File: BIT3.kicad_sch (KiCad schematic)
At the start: 39 parts, among them J1 Conn_02x04_Odd_Even, J2 Conn_01x02_Pin, Q1 2SC1815, SW1 SW_SPDT, SW2 SW_Push, SW3 SW_Push, U2 SG-107F, U3 SG-107F, U4 SG-107F, U5 SG-107F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

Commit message: Update PCB Design
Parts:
- added R17, R18, R19, R20, R21: R, Resistor_THT:R_Axial_DIN0204_L3.6mm_D1.6mm_P7.62mm_Horizontal, symbol Device:R
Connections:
- net +BATT: now also R17.1; no longer U7.8 (CH7)
- net GND: now also R21.2
- new net: R17.2, R18.1
- new net: R20.2, R21.1, U7.8 (CH7)
- new net: R18.2, R19.1
- new net: R19.2, R20.1
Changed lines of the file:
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@@
   (junction (at 163.83 127) (diameter 0) (color 0 0 0 0)
+  )
+  (junction (at 16.51 152.4) (diameter 0) (color 0 0 0 0)
   )
   (junction (at 97.79 143.51) (diameter 0) (color 0 0 0 0)
@@
     (stroke (width 0) (type default))
   )
+  (wire (pts (xy 16.51 152.4) (xy 36.83 152.4))
+    (stroke (width 0) (type default))
+  )
   (wire (pts (xy 88.9 76.2) (xy 91.44 76.2))
     (stroke (width 0) (type default))
@@
     (effects (font (size 1.27 1.27)) (justify right bottom))
   )
+  (label "V_Battery" (at 16.51 121.92 0) (fields_autoplaced)
+    (effects (font (size 1.27 1.27)) (justify left bottom))
+  )
   (label "DRV8835_AIN2" (at 147.32 101.6 180) (fields_autoplaced)
     (effects (font (size 1.27 1.27)) (justify right bottom))
@@
     (effects (font (size 1.27 1.27)) (justify left bottom))
   )
-  (label "V_Battery" (at 36.83 152.4 180) (fields_autoplaced)
-    (effects (font (size 1.27 1.27)) (justify right bottom))
-  )
   (label "LED_CL" (at 203.2 76.2 0) (fields_autoplaced)
     (effects (font (size 1.27 1.27)) (justify left bottom))
@@
     (pin "1")
     (pin "2")
+    (pin "3")
     (pin "4")
-    (pin "3")
     (instances
       (project "BIT3"
@@
         (path "/e911d5a5-765c-4e39-aa6a-9a13739432fd"
           (reference "R5") (unit 1)
+        )
+      )
+    )
+  )
+  (symbol (lib_id "power:GND") (at 16.51 160.02 0) (unit 1)
+    (in_bom yes) (on_board yes) (dnp no) (fields_autoplaced)
+    (property "Reference" "#PWR024" (at 16.51 166.37 0)
+      (effects (font (size 1.27 1.27)) hide)
+    )
+    (property "Value" "GND" (at 16.51 165.1 0)
+      (effects (font (size 1.27 1.27)))
+    )
+    (property "Footprint" "" (at 16.51 160.02 0)
+      (effects (font (size 1.27 1.27)) hide)
+    )
+    (property "Datasheet" "" (at 16.51 160.02 0)
+      (effects (font (size 1.27 1.27)) hide)
+    )
+    (pin "1")
+    (instances
+      (project "BIT3"
+        (path "/e911d5a5-765c-4e39-aa6a-9a13739432fd"
+          (reference "#PWR024") (unit 1)
+        )
+      )
+    )
+  )
+  (symbol (lib_id "Device:R") (at 16.51 125.73 0) (unit 1)
+    (in_bom yes) (on_board yes) (dnp no) (fields_autoplaced)
+    (property "Reference" "R17" (at 19.05 125.095 0)
+      (effects (font (size 1.27 1.27)) (justify left))
+    )
+    (property "Value" "R" (at 19.05 127.635 0)
+      (effects (font (size 1.27 1.27)) (justify left))
+    )
+    (property "Footprint" "Resistor_THT:R_Axial_DIN0204_L3.6mm_D1.6mm_P7.62mm_Horizontal" (at 14.732 125.73 90)
+      (effects (font (size 1.27 1.27)) hide)
+    )
+    (property "Datasheet" "~" (at 16.51 125.73 0)
+      (effects (font (size 1.27 1.27)) hide)
+    )
+    (pin "1")
+    (pin "2")
+    (instances
+      (project "BIT3"
+        (path "/e911d5a5-765c-4e39-aa6a-9a13739432fd"
+          (reference "R17") (unit 1)
         )
       )
@@
     )
   )
+  (symbol (lib_id "Device:R") (at 16.51 156.21 0) (unit 1)
+    (in_bom yes) (on_board yes) (dnp no) (fields_autoplaced)
+    (property "Reference" "R21" (at 19.05 155.575 0)
+      (effects (font (size 1.27 1.27)) (justify left))
+    )
+    (property "Value" "R" (at 19.05 158.115 0)
+      (effects (font (size 1.27 1.27)) (justify left))
+    )
+    (property "Footprint" "Resistor_THT:R_Axial_DIN0204_L3.6mm_D1.6mm_P7.62mm_Horizontal" (at 14.732 156.21 90)
+      (effects (font (size 1.27 1.27)) hide)
+    )
+    (property "Datasheet" "~" (at 16.51 156.21 0)
+      (effects (font (size 1.27 1.27)) hide)
+    )
+    (pin "1")
+    (pin "2")
+    (instances
+      (project "BIT3"
+        (path "/e911d5a5-765c-4e39-aa6a-9a13739432fd"
+          (reference "R21") (unit 1)
+        )
+      )
+    )
+  )
   (symbol (lib_id "Device:C") (at 233.68 128.27 0) (unit 1)
     (in_bom yes) (on_board yes) (dnp no) (fields_autoplaced)
@@
         (path "/e911d5a5-765c-4e39-aa6a-9a13739432fd"
           (reference "U4") (unit 1)
+        )
+      )
+    )
+  )
+  (symbol (lib_id "Device:R") (at 16.51 133.35 0) (unit 1)
+    (in_bom yes) (on_board yes) (dnp no) (fields_autoplaced)
+    (property "Reference" "R18" (at 19.05 132.715 0)
+      (effects (font (size 1.27 1.27)) (justify left))
+    )
+    (property "Value" "R" (at 19.05 135.255 0)
+      (effects (font (size 1.27 1.27)) (justify left))
+    )
+    (property "Footprint" "Resistor_THT:R_Axial_DIN0204_L3.6mm_D1.6mm_P7.62mm_Horizontal" (at 14.732 133.35 90)
+      (effects (font (size 1.27 1.27)) hide)
+    )
+    (property "Datasheet" "~" (at 16.51 133.35 0)
+      (effects (font (size 1.27 1.27)) hide)
+    )
+    (pin "1")
+    (pin "2")
+    (instances
+      (project "BIT3"
+        (path "/e911d5a5-765c-4e39-aa6a-9a13739432fd"
+          (reference "R18") (unit 1)
         )
       )
@@
     )
   )
+  (symbol (lib_id "Device:R") (at 16.51 148.59 0) (unit 1)
+    (in_bom yes) (on_board yes) (dnp no) (fields_autoplaced)
+    (property "Reference" "R20" (at 19.05 147.955 0)
+      (effects (font (size 1.27 1.27)) (justify left))
+    )
+    (property "Value" "R" (at 19.05 150.495 0)
+      (effects (font (size 1.27 1.27)) (justify left))
+    )
+    (property "Footprint" "Resistor_THT:R_Axial_DIN0204_L3.6mm_D1.6mm_P7.62mm_Horizontal" (at 14.732 148.59 90)
+      (effects (font (size 1.27 1.27)) hide)
+    )
+    (property "Datasheet" "~" (at 16.51 148.59 0)
+      (effects (font (size 1.27 1.27)) hide)
+    )
+    (pin "1")
+    (pin "2")
+    (instances
+      (project "BIT3"
+        (path "/e911d5a5-765c-4e39-aa6a-9a13739432fd"
+          (reference "R20") (unit 1)
+        )
+      )
+    )
+  )
   (symbol (lib_id "Device:R") (at 226.06 80.01 0) (unit 1)
     (in_bom yes) (on_board yes) (dnp no) (fields_autoplaced)
@@
         )
       )
+    )
+  )
+  (symbol (lib_id "Device:R") (at 16.51 140.97 0) (unit 1)
+    (in_bom yes) (on_board yes) (dnp no) (fields_autoplaced)
+    (property "Reference" "R19" (at 19.05 140.335 0)
+      (effects (font (size 1.27 1.27)) (justify left))
+    )
+    (property "Value" "R" (at 19.05 142.875 0)
+      (effects (font (size 1.27 1.27)) (justify left))
+    )
+    (property "Footprint" "Resistor_THT:R_Axial_DIN0204_L3.6mm_D1.6mm_P7.62mm_Horizontal" (at 14.732 140.97 90)
+      (effects (font (size 1.27 1.27)) hide)
+    )
+    (property "Datasheet" "~" (at 16.51 140.97 0)
+      (effects (font (size 1.27 1.27)) hide)
+    )
+    (pin "1")
+    (pin "2")
+    (instances
+      (project "BIT3"
+        (path "/e911d5a5-765c-4e39-aa6a-9a13739432fd"
+          (reference "R19") (unit 1)
+        )
+      )

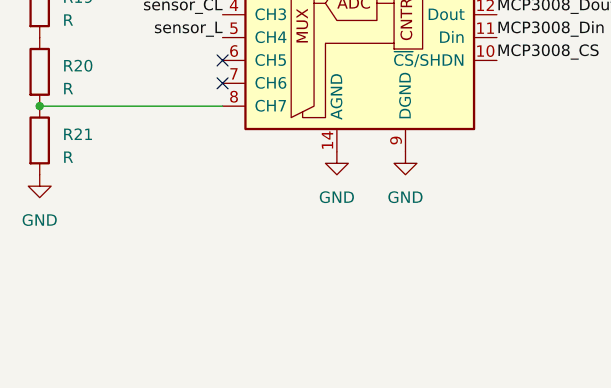
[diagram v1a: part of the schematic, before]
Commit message: 基板更新
MCP3008 にパスコンを追加
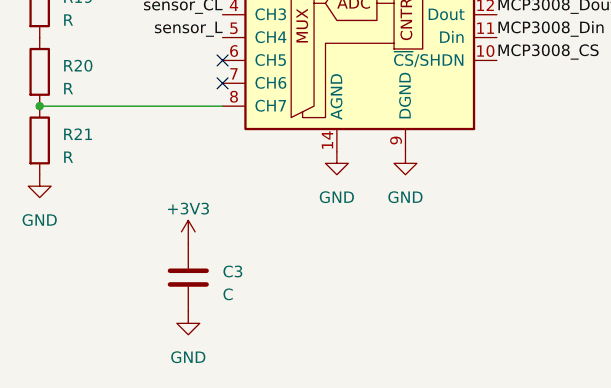
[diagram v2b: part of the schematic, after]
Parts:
- added C3: C, Capacitor_THT:C_Disc_D4.7mm_W2.5mm_P5.00mm, symbol Device:C
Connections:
- net +3V3: now also C3.1
- net GND: now also C3.2
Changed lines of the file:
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@@
+    )
+  )
+  (symbol (lib_id "power:+3V3") (at 33.02 167.64 0) (unit 1)
+    (in_bom yes) (on_board yes) (dnp no) (fields_autoplaced)
+    (property "Reference" "#PWR027" (at 33.02 171.45 0)
+      (effects (font (size 1.27 1.27)) hide)
+    )
+    (property "Value" "+3V3" (at 33.02 163.83 0)
+      (effects (font (size 1.27 1.27)))
+    )
+    (property "Footprint" "" (at 33.02 167.64 0)
+      (effects (font (size 1.27 1.27)) hide)
+    )
+    (property "Datasheet" "" (at 33.02 167.64 0)
+      (effects (font (size 1.27 1.27)) hide)
+    )
+    (pin "1")
+    (instances
+      (project "RP2040-BasicDesign"
+        (path "/14b941fc-8df0-4613-ad34-21e1e03e5f30"
+          (reference "#PWR027") (unit 1)
+        )
+      )
+      (project "BIT3"
+        (path "/e911d5a5-765c-4e39-aa6a-9a13739432fd"
+          (reference "#PWR025") (unit 1)
+        )
+      )
     )
   )
@@
         (path "/e911d5a5-765c-4e39-aa6a-9a13739432fd"
           (reference "#PWR08") (unit 1)
+        )
+      )
+    )
+  )
+  (symbol (lib_id "Device:C") (at 33.02 171.45 0) (unit 1)
+    (in_bom yes) (on_board yes) (dnp no) (fields_autoplaced)
+    (property "Reference" "C3" (at 36.83 170.815 0)
+      (effects (font (size 1.27 1.27)) (justify left))
+    )
+    (property "Value" "C" (at 36.83 173.355 0)
+      (effects (font (size 1.27 1.27)) (justify left))
+    )
+    (property "Footprint" "Capacitor_THT:C_Disc_D4.7mm_W2.5mm_P5.00mm" (at 33.9852 175.26 0)
+      (effects (font (size 1.27 1.27)) hide)
+    )
+    (property "Datasheet" "~" (at 33.02 171.45 0)
+      (effects (font (size 1.27 1.27)) hide)
+    )
+    (pin "1")
+    (pin "2")
+    (instances
+      (project "BIT3"
+        (path "/e911d5a5-765c-4e39-aa6a-9a13739432fd"
+          (reference "C3") (unit 1)
         )
       )
@@
         )
       )
+    )
+  )
+  (symbol (lib_id "power:GND") (at 33.02 175.26 0) (unit 1)
+    (in_bom yes) (on_board yes) (dnp no) (fields_autoplaced)
+    (property "Reference" "#PWR026" (at 33.02 181.61 0)
+      (effects (font (size 1.27 1.27)) hide)
+    )
+    (property "Value" "GND" (at 33.02 180.34 0)
+      (effects (font (size 1.27 1.27)))
+    )
+    (property "Footprint" "" (at 33.02 175.26 0)
+      (effects (font (size 1.27 1.27)) hide)
+    )
+    (property "Datasheet" "" (at 33.02 175.26 0)
+      (effects (font (size 1.27 1.27)) hide)
+    )
+    (pin "1")
+    (instances
+      (project "BIT3"
+        (path "/e911d5a5-765c-4e39-aa6a-9a13739432fd"
+          (reference "#PWR026") (unit 1)
+        )
+      )

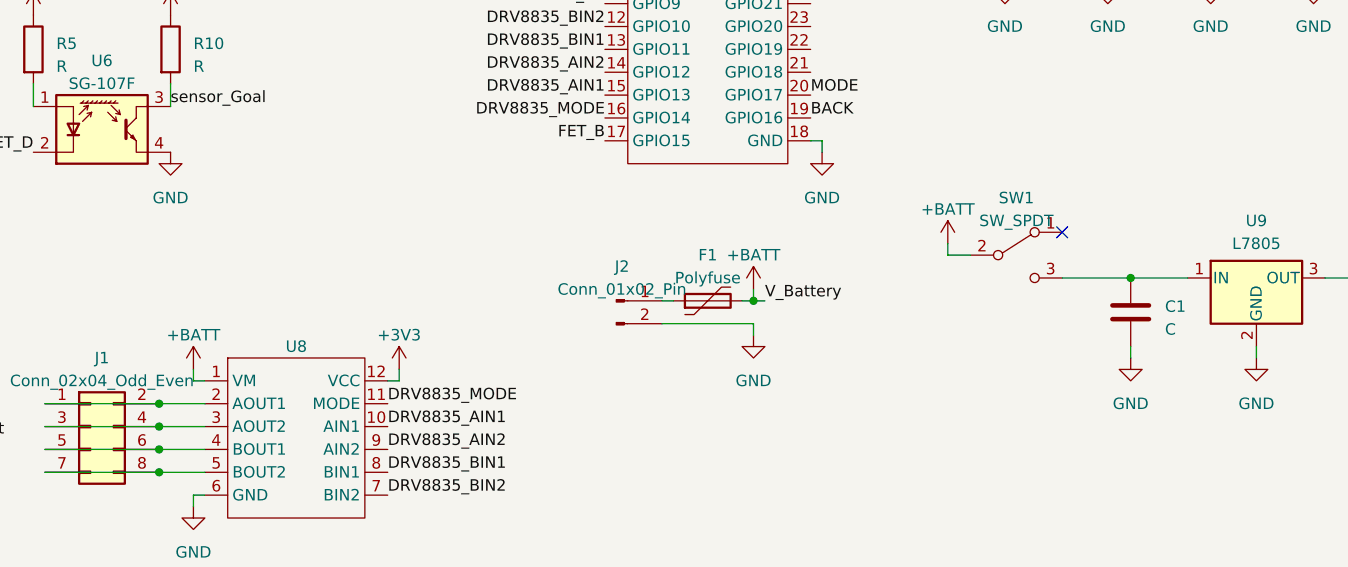
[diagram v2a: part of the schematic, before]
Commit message: 逆説防止 D を追加, バッテリ電圧監視 ADC の配置を変更
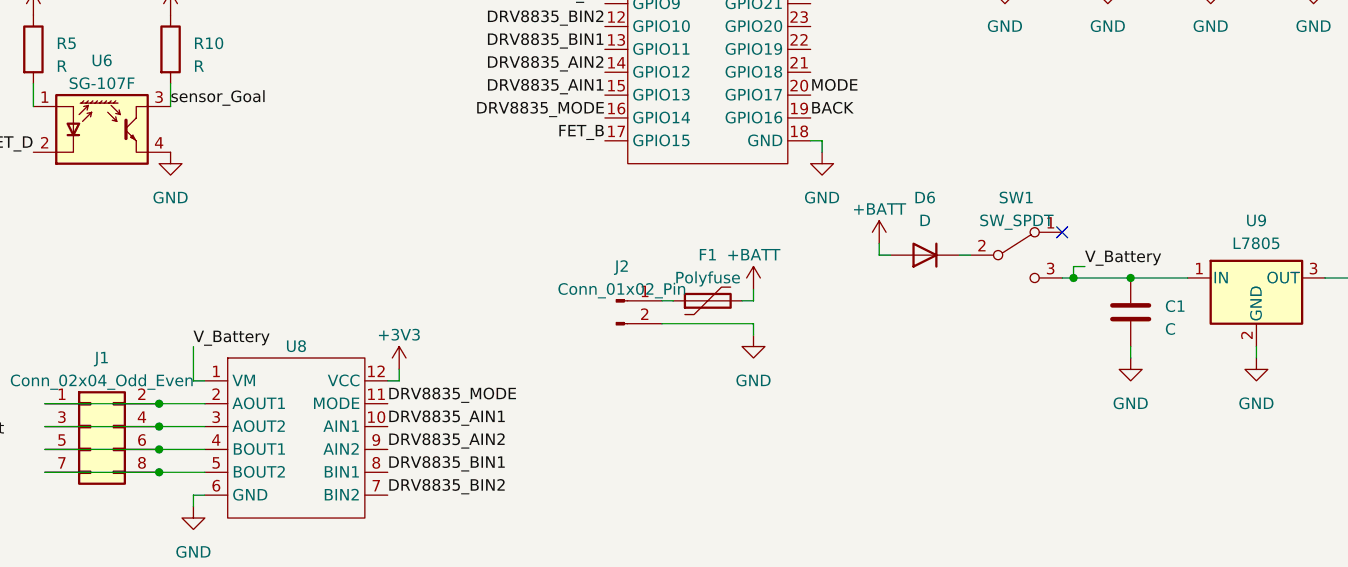
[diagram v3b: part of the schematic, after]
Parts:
- added D6: D, Diode_THT:D_A-405_P7.62mm_Horizontal, symbol Device:D
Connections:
- net +BATT: now also D6.2 (A); no longer R17.1, SW1.2 (B), U8.1 (VM)
- net V_Battery: now reaches C1.1, SW1.3 (C), U9.1 (IN)
- net V_Battery: now also R17.1, U8.1 (VM)
- new net: D6.1 (K), SW1.2 (B)
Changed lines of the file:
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@@
   (junction (at 233.68 124.46) (diameter 0) (color 0 0 0 0)
   )
+  (junction (at 199.39 124.46) (diameter 0) (color 0 0 0 0)
+  )
   (junction (at 205.74 124.46) (diameter 0) (color 0 0 0 0)
-  )
-  (junction (at 163.83 127) (diameter 0) (color 0 0 0 0)
   )
   (junction (at 16.51 152.4) (diameter 0) (color 0 0 0 0)
@@
     (stroke (width 0) (type default))
   )
-  (wire (pts (xy 185.42 120.65) (xy 185.42 121.92))
+  (wire (pts (xy 177.8 120.65) (xy 177.8 121.92))
     (stroke (width 0) (type default))
   )
@@
     (stroke (width 0) (type default))
   )
+  (wire (pts (xy 200.66 123.19) (xy 199.39 123.19))
+    (stroke (width 0) (type default))
+  )
   (wire (pts (xy 147.32 68.58) (xy 146.05 68.58))
     (stroke (width 0) (type default))
   )
-  (wire (pts (xy 185.42 121.92) (xy 187.96 121.92))
-    (stroke (width 0) (type default))
-  )
   (wire (pts (xy 102.87 135.89) (xy 101.6 135.89))
     (stroke (width 0) (type default))
@@
     (stroke (width 0) (type default))
   )
-  (wire (pts (xy 101.6 135.89) (xy 101.6 134.62))
+  (wire (pts (xy 101.6 135.89) (xy 101.6 132.08))
     (stroke (width 0) (type default))
   )
@@
     (stroke (width 0) (type default))
   )
+  (wire (pts (xy 177.8 121.92) (xy 179.07 121.92))
+    (stroke (width 0) (type default))
+  )
   (wire (pts (xy 171.45 110.49) (xy 171.45 109.22))
     (stroke (width 0) (type default))
@@
     (stroke (width 0) (type default))
   )
-  (wire (pts (xy 165.1 127) (xy 163.83 127))
-    (stroke (width 0) (type default))
-  )
   (wire (pts (xy 219.71 132.08) (xy 219.71 133.35))
     (stroke (width 0) (type default))
   )
+  (wire (pts (xy 199.39 124.46) (xy 205.74 124.46))
+    (stroke (width 0) (type default))
+  )
   (wire (pts (xy 97.79 146.05) (xy 102.87 146.05))
     (stroke (width 0) (type default))
@@
     (stroke (width 0) (type default))
   )
-  (wire (pts (xy 198.12 124.46) (xy 205.74 124.46))
+  (wire (pts (xy 199.39 123.19) (xy 199.39 124.46))
+    (stroke (width 0) (type default))
+  )
+  (wire (pts (xy 198.12 124.46) (xy 199.39 124.46))
     (stroke (width 0) (type default))
   )
   (wire (pts (xy 99.06 68.58) (xy 99.06 71.12))
     (stroke (width 0) (type default))
+  )
+  (wire (pts (xy 186.69 121.92) (xy 187.96 121.92))
+    (stroke (width 0) (type default))
+  )
+  (label "V_Battery" (at 200.66 123.19 0) (fields_autoplaced)
+    (effects (font (size 1.27 1.27)) (justify left bottom))
   )
   (label "sensor_CR" (at 71.12 77.47 0) (fields_autoplaced)
@@
     (effects (font (size 1.27 1.27)) (justify right bottom))
   )
-  (label "V_Battery" (at 165.1 127 0) (fields_autoplaced)
-    (effects (font (size 1.27 1.27)) (justify left bottom))
-  )
   (label "LED_Goal" (at 237.49 76.2 0) (fields_autoplaced)
     (effects (font (size 1.27 1.27)) (justify left bottom))
@@
   (label "LED_R" (at 147.32 73.66 180) (fields_autoplaced)
     (effects (font (size 1.27 1.27)) (justify right bottom))
+  )
+  (label "V_Battery" (at 101.6 132.08 0) (fields_autoplaced)
+    (effects (font (size 1.27 1.27)) (justify left bottom))
   )
   (label "sensor_Goal" (at 99.06 105.41 0) (fields_autoplaced)
@@
     )
   )
-  (symbol (lib_id "power:+BATT") (at 185.42 120.65 0) (unit 1)
-    (in_bom yes) (on_board yes) (dnp no) (fields_autoplaced)
-    (property "Reference" "#PWR019" (at 185.42 124.46 0)
-      (effects (font (size 1.27 1.27)) hide)
-    )
-    (property "Value" "+BATT" (at 185.42 116.84 0)
-      (effects (font (size 1.27 1.27)))
-    )
-    (property "Footprint" "" (at 185.42 120.65 0)
-      (effects (font (size 1.27 1.27)) hide)
-    )
-    (property "Datasheet" "" (at 185.42 120.65 0)
+  (symbol (lib_id "power:+BATT") (at 177.8 120.65 0) (unit 1)
+    (in_bom yes) (on_board yes) (dnp no) (fields_autoplaced)
+    (property "Reference" "#PWR019" (at 177.8 124.46 0)
+      (effects (font (size 1.27 1.27)) hide)
+    )
+    (property "Value" "+BATT" (at 177.8 116.84 0)
+      (effects (font (size 1.27 1.27)))
+    )
+    (property "Footprint" "" (at 177.8 120.65 0)
+      (effects (font (size 1.27 1.27)) hide)
+    )
+    (property "Datasheet" "" (at 177.8 120.65 0)
       (effects (font (size 1.27 1.27)) hide)
     )
@@
     )
   )
-  (symbol (lib_id "power:+BATT") (at 101.6 134.62 0) (unit 1)
-    (in_bom yes) (on_board yes) (dnp no) (fields_autoplaced)
-    (property "Reference" "#PWR05" (at 101.6 138.43 0)
-      (effects (font (size 1.27 1.27)) hide)
-    )
-    (property "Value" "+BATT" (at 101.6 130.81 0)
-      (effects (font (size 1.27 1.27)))
-    )
-    (property "Footprint" "" (at 101.6 134.62 0)
-      (effects (font (size 1.27 1.27)) hide)
-    )
-    (property "Datasheet" "" (at 101.6 134.62 0)
-      (effects (font (size 1.27 1.27)) hide)
-    )
-    (pin "1")
-    (instances
-      (project "BIT3"
-        (path "/e911d5a5-765c-4e39-aa6a-9a13739432fd"
-          (reference "#PWR05") (unit 1)
-        )
-      )
-    )
-  )
   (symbol (lib_id "power:GND") (at 163.83 130.81 0) (unit 1)
     (in_bom yes) (on_board yes) (dnp no) (fields_autoplaced)
@@
         )
       )
+    )
+  )
+  (symbol (lib_id "Device:D") (at 182.88 121.92 180) (unit 1)
+    (in_bom yes) (on_board yes) (dnp no) (fields_autoplaced)
+    (property "Reference" "D6" (at 182.88 115.57 0)
+      (effects (font (size 1.27 1.27)))
+    )
+    (property "Value" "D" (at 182.88 118.11 0)
+      (effects (font (size 1.27 1.27)))
+    )
+    (property "Footprint" "Diode_THT:D_A-405_P7.62mm_Horizontal" (at 182.88 121.92 0)
+      (effects (font (size 1.27 1.27)) hide)
+    )
+    (property "Datasheet" "~" (at 182.88 121.92 0)
+      (effects (font (size 1.27 1.27)) hide)
+    )
+    (property "Sim.Device" "D" (at 182.88 121.92 0)
+      (effects (font (size 1.27 1.27)) hide)
+    )
+    (property "Sim.Pins" "1=K 2=A" (at 182.88 121.92 0)
+      (effects (font (size 1.27 1.27)) hide)
+    )
+    (pin "1")
+    (pin "2")
+    (instances
+      (project "BIT3"
+        (path "/e911d5a5-765c-4e39-aa6a-9a13739432fd"
+          (reference "D6") (unit 1)
+        )
+      )
